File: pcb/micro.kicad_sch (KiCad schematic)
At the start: 1 part, among them U1 ESP32-S3

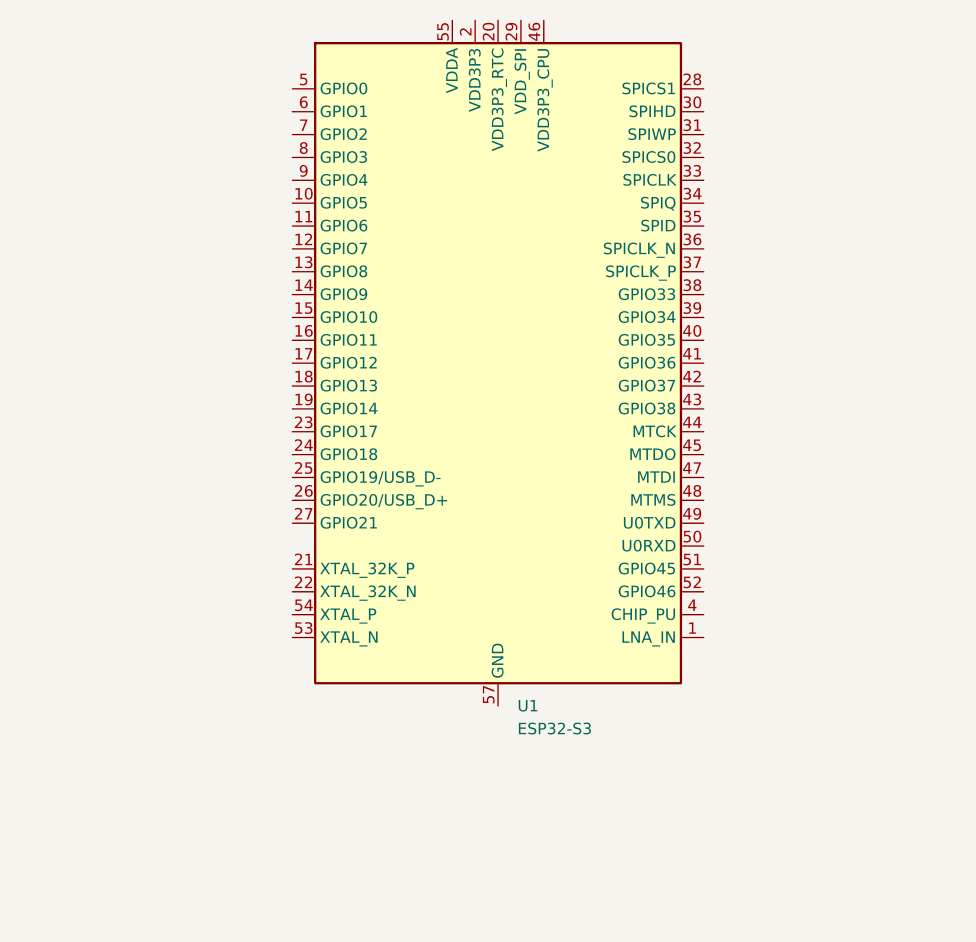
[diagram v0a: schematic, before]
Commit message: Finished most of schematic
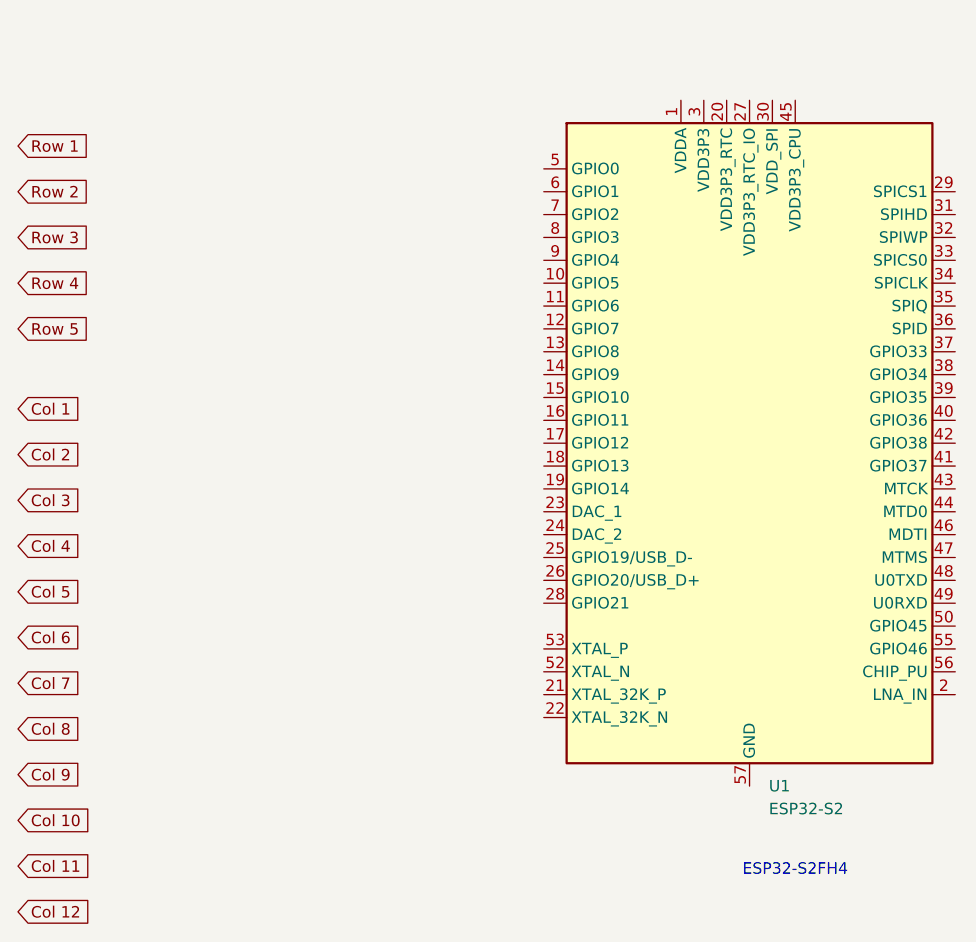
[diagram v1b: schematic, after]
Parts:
- removed U1: ESP32-S3, Package_DFN_QFN:QFN-56-1EP_7x7mm_P0.4mm_EP4x4mm, symbol MCU_Espressif:ESP32-S3
- added U1: ESP32-S2, Package_DFN_QFN:QFN-56-1EP_7x7mm_P0.4mm_EP4x4mm, symbol MCU_Espressif:ESP32-S2
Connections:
- new net: U1.1 (VDDA), U1.51 (VDDA), U1.54 (VDDA)
- new net: U1.3 (VDD3P3), U1.4 (VDD3P3)
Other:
- note added: "ESP32-S2FH4"

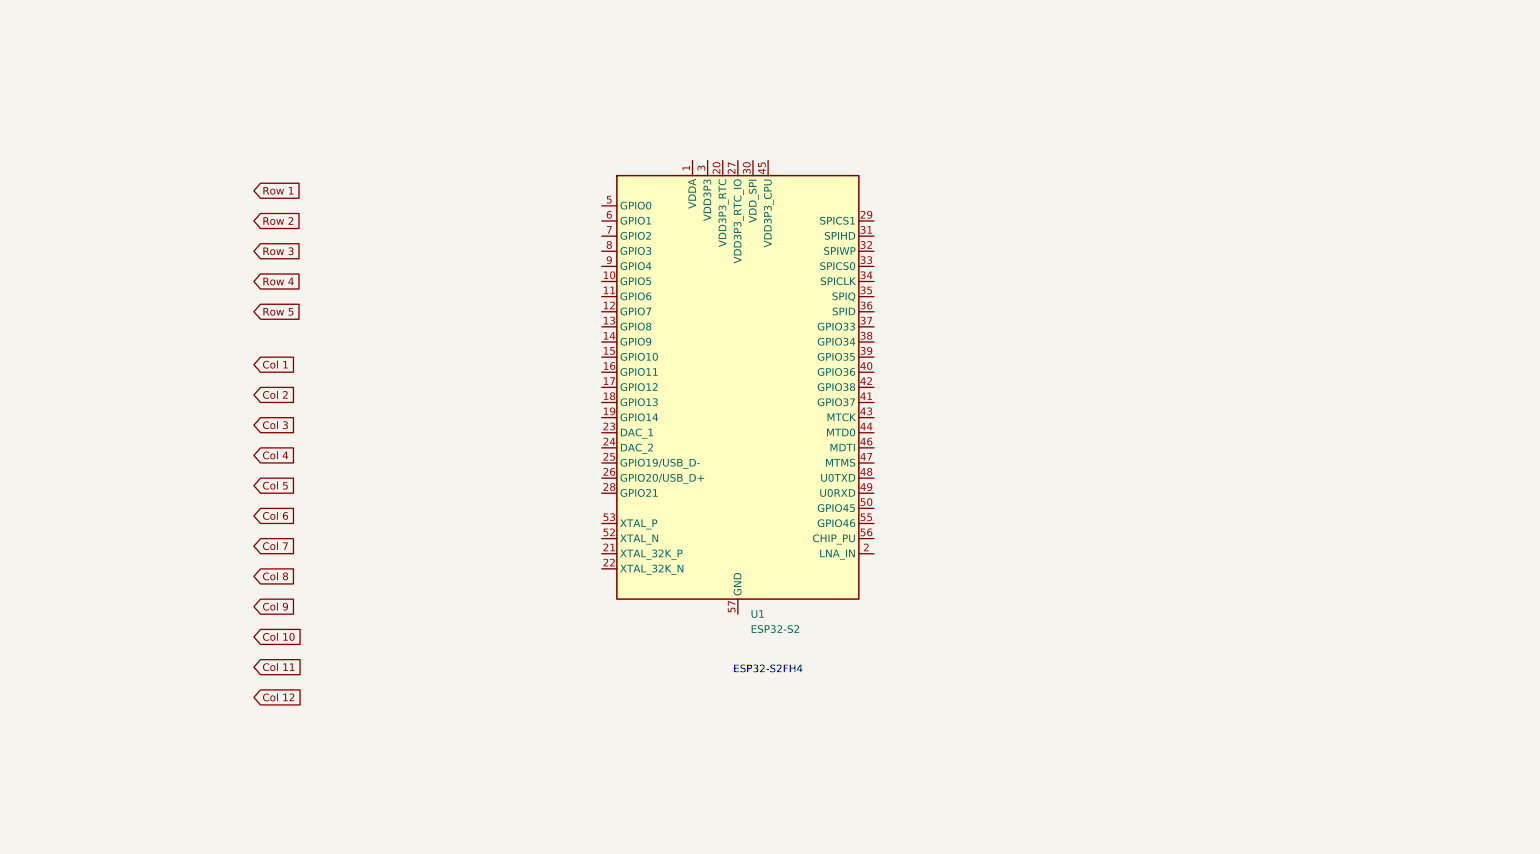
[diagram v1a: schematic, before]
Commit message: Finished main component selection
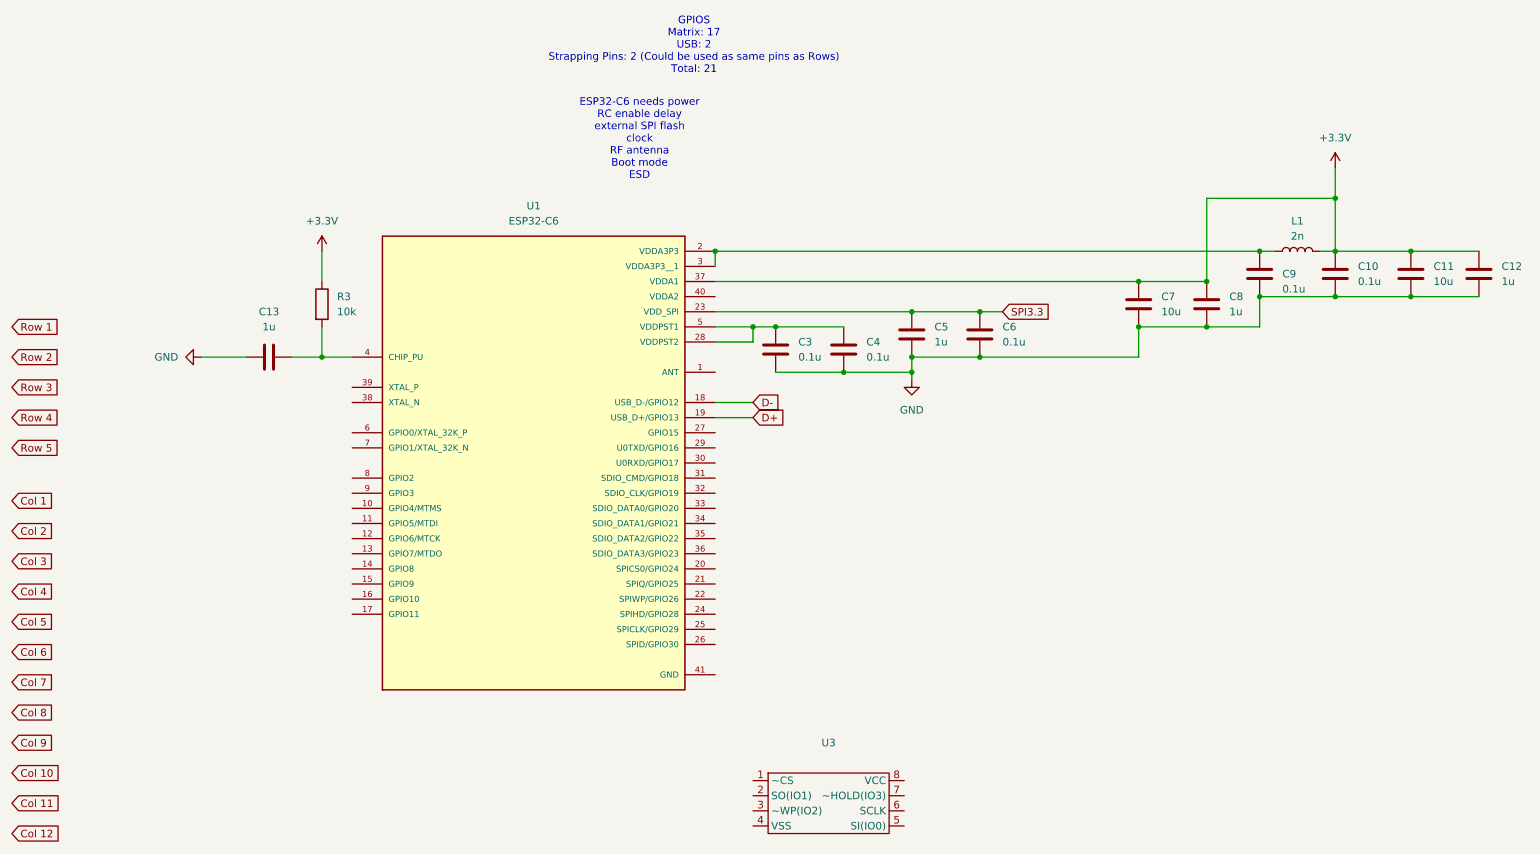
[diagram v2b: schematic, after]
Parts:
- removed U1: ESP32-S2, Package_DFN_QFN:QFN-56-1EP_7x7mm_P0.4mm_EP4x4mm, symbol MCU_Espressif:ESP32-S2
- added C10, C3, C4, C6, C9: 0.1u, Resistor_SMD:R_0402_1005Metric_Pad0.72x0.64mm_HandSolder, symbol Device:C
- added C11, C7: 10u, Resistor_SMD:R_0402_1005Metric_Pad0.72x0.64mm_HandSolder, symbol Device:C
- added C12, C5, C8: 1u, Resistor_SMD:R_0402_1005Metric_Pad0.72x0.64mm_HandSolder, symbol Device:C
- added C13: 1u, Capacitor_SMD:C_0402_1005Metric_Pad0.74x0.62mm_HandSolder, symbol Device:C
- added L1: 2n, Inductor_SMD:L_0402_1005Metric_Pad0.77x0.64mm_HandSolder, symbol Device:L
- added R3: 10k, Resistor_SMD:R_0402_1005Metric_Pad0.72x0.64mm_HandSolder, symbol Device:R
- added U1: ESP32-C6, ESP32:QFN40P500X500X90-41N, symbol ESP32:ESP32-C6
- added U3: ~, ESP32:SOIC127P790X216-8N, symbol ESP32:GD25Q32ESIGR
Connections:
- new net: C13.1, R3.2, U1.4 (CHIP_PU)
- new net: C9.1, L1.1, U1.2 (VDDA3P3), U1.3 (VDDA3P3__1)
- new net: C3.1, C4.1, U1.28 (VDDPST2), U1.5 (VDDPST1)
- new net +3.3V: C10.1, C11.1, C12.1, C7.1, C8.1, L1.2, R3.1, U1.37 (VDDA1)
- new net D+: U1.19 (USB_D+/GPIO13)
- new net D-: U1.18 (USB_D-/GPIO12)
- new net GND: C10.2, C11.2, C12.2, C13.2, C3.2, C4.2, C5.2, C6.2, C7.2, C8.2, C9.2
- new net SPI3.3: C5.1, C6.1, U1.23 (VDD_SPI)
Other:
- note added: "ESP32-C6 needs power RC enable delay external SPI flash clock RF antenna Boot mode ESD"
- note added: "GPIOS Matrix: 17 USB: 2 Strapping Pins: 2 (Could be used as same pins as Rows) Total: 21"
- note removed: "ESP32-S2FH4"
